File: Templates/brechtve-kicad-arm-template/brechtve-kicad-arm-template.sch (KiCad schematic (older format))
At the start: 16 parts, among them J1 DebugHeader_Cortex-M_SWD_UART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, J2 DebugHeader_Cortex-M_JTAG_10p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, J3 DebugHeader_UART_4p, SW1 SW_Push

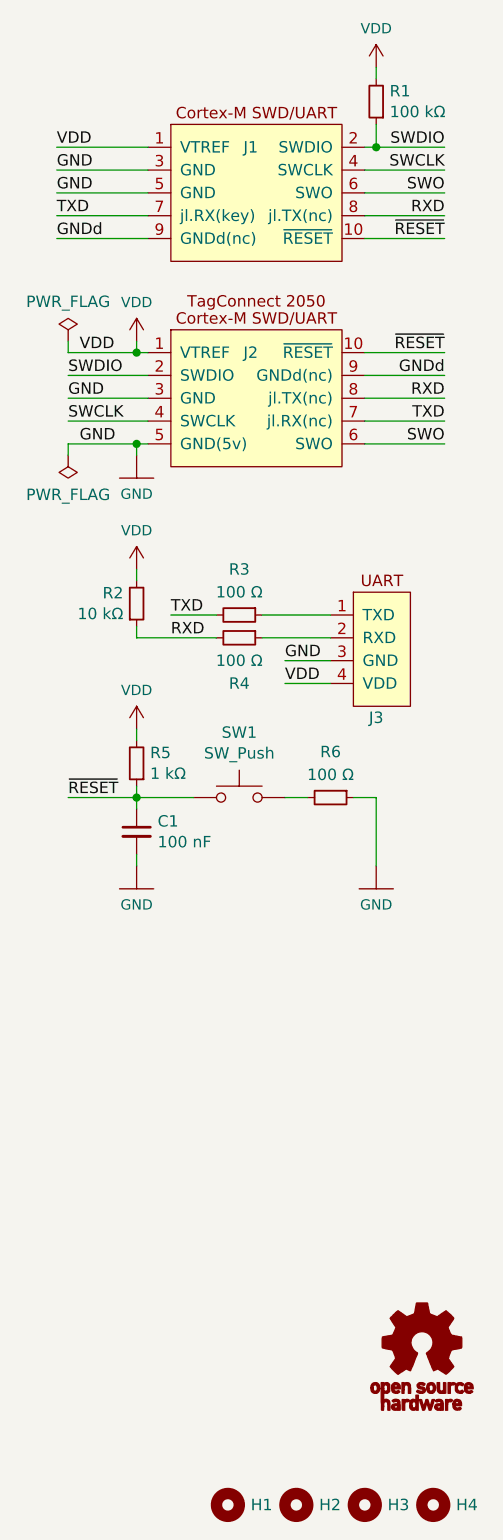
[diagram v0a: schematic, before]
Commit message: Updated power symbol positions
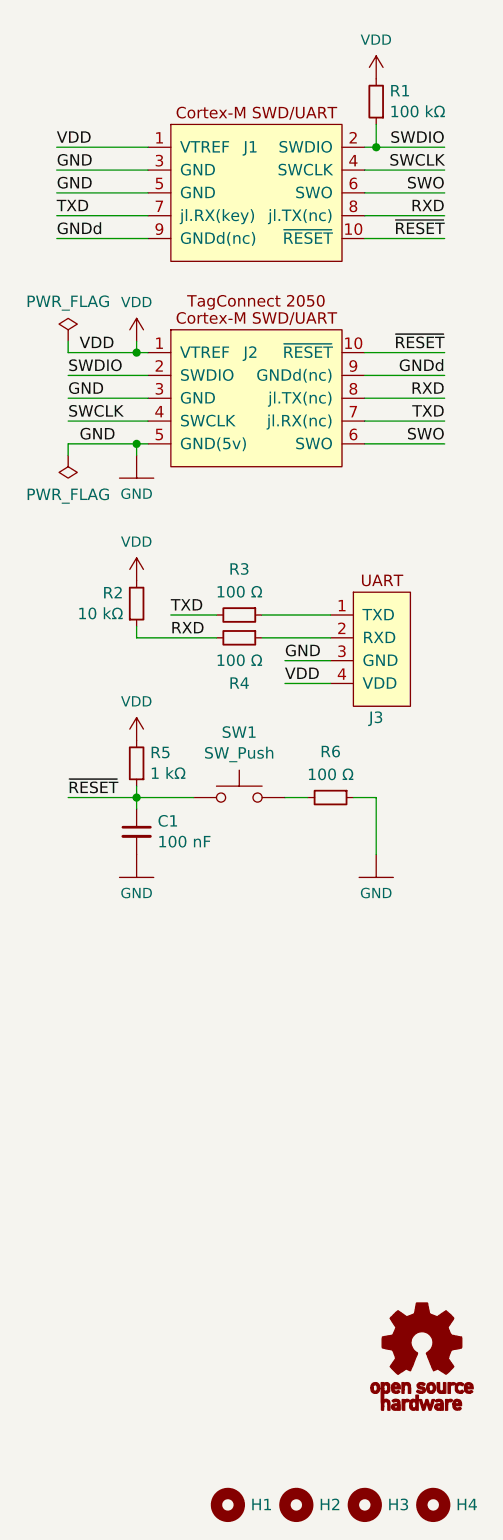
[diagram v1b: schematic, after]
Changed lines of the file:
@@
 L SparkFun-PowerSymbols:VDD #SUPPLY0102
 U 1 1 5E4FCF2A
-P 9700 2950
-F 0 "#SUPPLY0102" H 9750 2950 45  0001 L BNN
-F 1 "VDD" H 9700 3120 45  0000 C CNN
-F 2 "XXX-00000" H 9700 3131 60  0001 C CNN
-F 3 "" H 9700 2950 60  0001 C CNN
-	1    9700 2950
+P 9700 3000
+F 0 "#SUPPLY0102" H 9750 3000 45  0001 L BNN
+F 1 "VDD" H 9700 3170 45  0000 C CNN
+F 2 "XXX-00000" H 9700 3181 60  0001 C CNN
+F 3 "" H 9700 3000 60  0001 C CNN
+	1    9700 3000
 	1    0    0    -1
 $EndComp
@@
 L SparkFun-PowerSymbols:VDD #SUPPLY0103
 U 1 1 5E506F4B
-P 10750 750
-F 0 "#SUPPLY0103" H 10800 750 45  0001 L BNN
-F 1 "VDD" H 10750 920 45  0000 C CNN
-F 2 "XXX-00000" H 10750 931 60  0001 C CNN
-F 3 "" H 10750 750 60  0001 C CNN
-	1    10750 750
+P 10750 800
+F 0 "#SUPPLY0103" H 10800 800 45  0001 L BNN
+F 1 "VDD" H 10750 970 45  0000 C CNN
+F 2 "XXX-00000" H 10750 981 60  0001 C CNN
+F 3 "" H 10750 800 60  0001 C CNN
+	1    10750 800
 	1    0    0    -1
 $EndComp
@@
 	-1   0    0    1
 $EndComp
-Wire Wire Line
-	9700 2950 9700 3000
-Wire Wire Line
-	10750 750  10750 800
 $Comp
 L Switch:SW_Push SW1
@@
 L SparkFun-PowerSymbols:VDD #SUPPLY0104
 U 1 1 5E51C73F
-P 9700 3650
-F 0 "#SUPPLY0104" H 9750 3650 45  0001 L BNN
-F 1 "VDD" H 9700 3820 45  0000 C CNN
-F 2 "XXX-00000" H 9700 3831 60  0001 C CNN
-F 3 "" H 9700 3650 60  0001 C CNN
-	1    9700 3650
+P 9700 3700
+F 0 "#SUPPLY0104" H 9750 3700 45  0001 L BNN
+F 1 "VDD" H 9700 3870 45  0000 C CNN
+F 2 "XXX-00000" H 9700 3881 60  0001 C CNN
+F 3 "" H 9700 3700 60  0001 C CNN
+	1    9700 3700
 	1    0    0    -1
 $EndComp
@@
 L SparkFun-PowerSymbols:GND #GND0102
 U 1 1 5E51C967
-P 10750 4250
-F 0 "#GND0102" H 10800 4200 45  0001 L BNN
-F 1 "GND" H 10750 4080 45  0000 C CNN
-F 2 "" H 10750 4150 60  0001 C CNN
-F 3 "" H 10750 4150 60  0001 C CNN
-	1    10750 4250
+P 10750 4200
+F 0 "#GND0102" H 10800 4150 45  0001 L BNN
+F 1 "GND" H 10750 4030 45  0000 C CNN
+F 2 "" H 10750 4100 60  0001 C CNN
+F 3 "" H 10750 4100 60  0001 C CNN
+	1    10750 4200
 	1    0    0    -1
 $EndComp
@@
 L SparkFun-PowerSymbols:GND #GND0103
 U 1 1 5E539A2B
-P 9700 4250
-F 0 "#GND0103" H 9750 4200 45  0001 L BNN
-F 1 "GND" H 9700 4080 45  0000 C CNN
-F 2 "" H 9700 4150 60  0001 C CNN
-F 3 "" H 9700 4150 60  0001 C CNN
-	1    9700 4250
+P 9700 4200
+F 0 "#GND0103" H 9750 4150 45  0001 L BNN
+F 1 "GND" H 9700 4030 45  0000 C CNN
+F 2 "" H 9700 4100 60  0001 C CNN
+F 3 "" H 9700 4100 60  0001 C CNN
+	1    9700 4200
 	1    0    0    -1
 $EndComp
-Wire Wire Line
-	9700 3650 9700 3700
 Wire Wire Line
 	9700 3900 9700 3950
@@
 	9700 3950 9700 4000
 Wire Wire Line
-	9700 4200 9700 4250
-Wire Wire Line
 	10350 3950 10450 3950
 Wire Wire Line
 	10650 3950 10750 3950
 Wire Wire Line
-	10750 3950 10750 4250
+	10750 3950 10750 4200
 Wire Wire Line
 	9350 1400 9750 1400
